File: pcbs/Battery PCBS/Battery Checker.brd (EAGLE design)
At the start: 49.5 x 49.5 mm, 19 parts

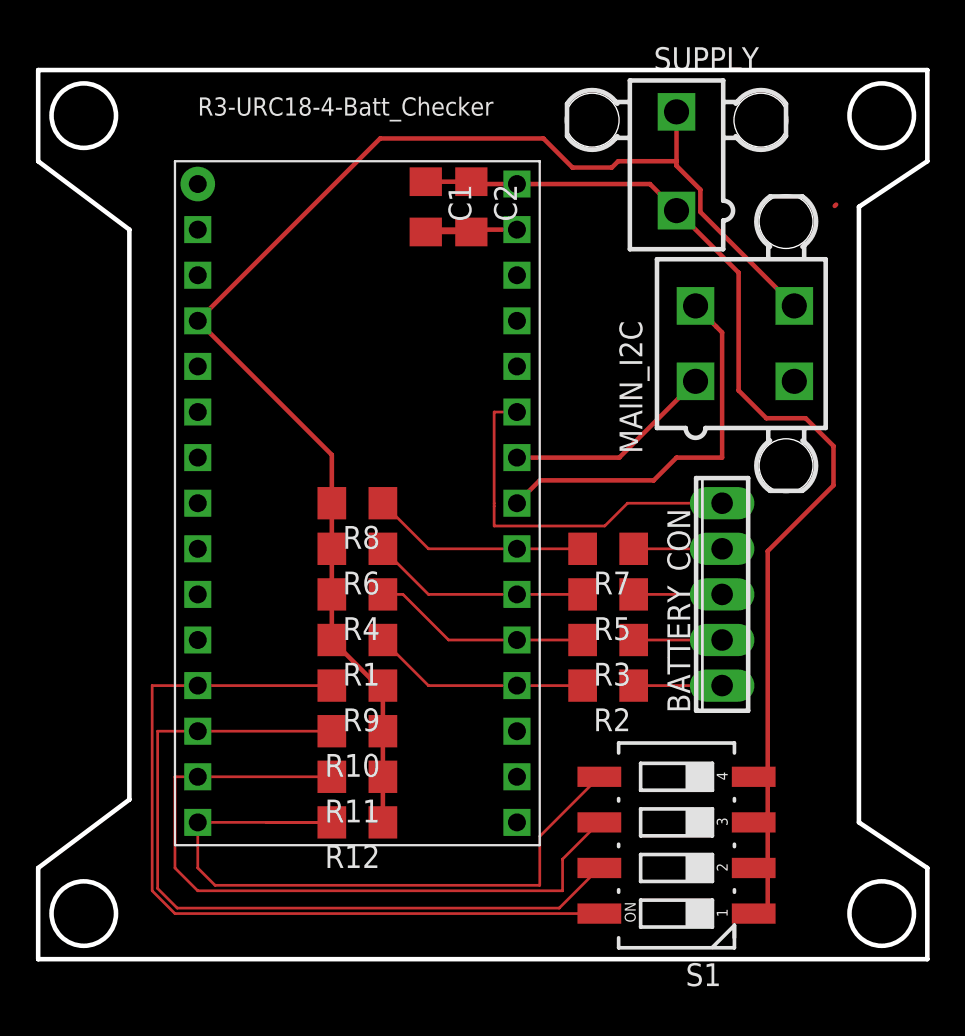
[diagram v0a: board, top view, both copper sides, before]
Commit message: added logic level converter
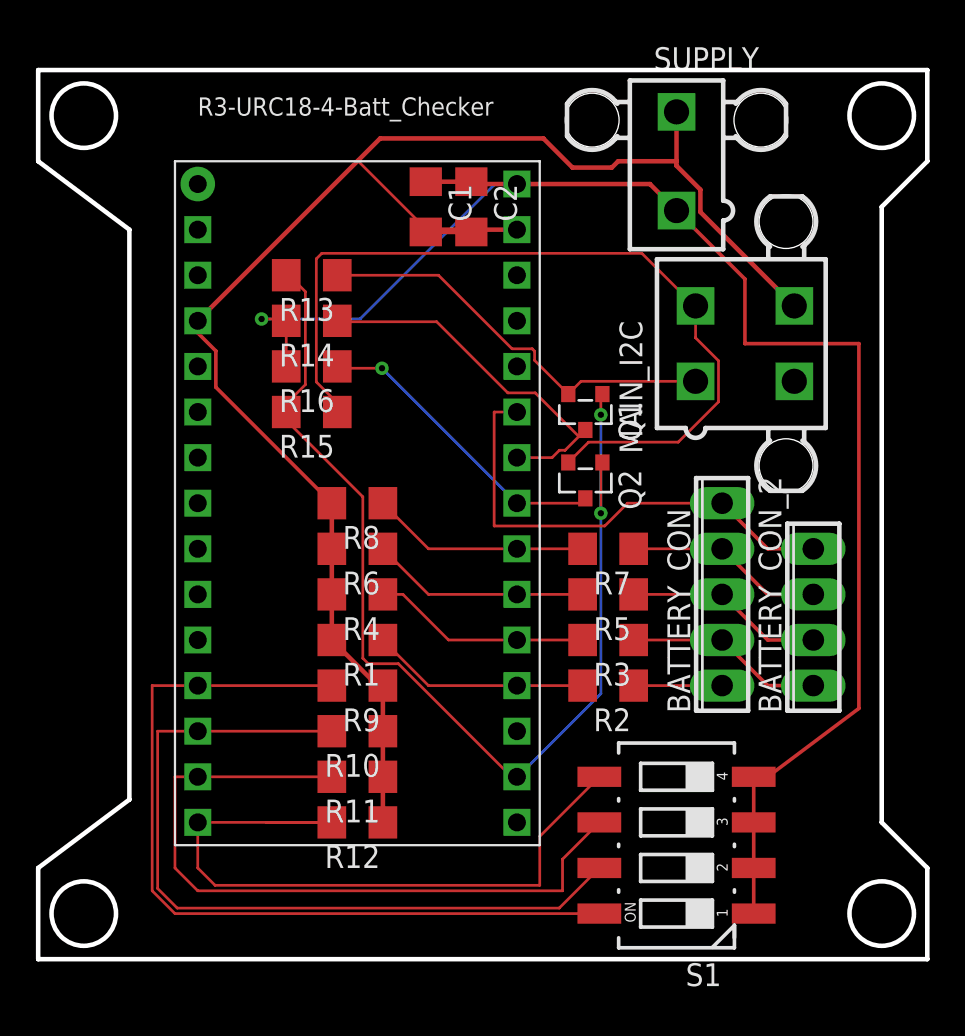
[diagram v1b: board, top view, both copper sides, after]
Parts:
- added BATTERY_CON_2: (no value), con-phoenix-254:4POL254
- added Q1, Q2: BSS138, bss138_10:SOT23
- added R13, R14, R15, R16: 10k, rcl:R1206
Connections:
- removed net 3.3V: U$1.3.3V
- new net 3.3: Q1.1, Q2.1, R13.2, R15.2, U$1.3.3V
- new net SCL_HV: Q1.3, R14.1, U$1.A5
- new net SDA_HV: Q2.3, R16.1, U$1.A4
- net BATT2: now also BATTERY_CON_2.1
- net BATT3: now also BATTERY_CON_2.2
- net BATT4: now also BATTERY_CON_2.3
- net BATT5: now also BATTERY_CON_2.4
- net SCL: now also Q1.2, R13.1; no longer U$1.A5
- net SDA: now also Q2.2, R15.1; no longer U$1.A4
- net VIN: now also R14.2, R16.2
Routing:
- net 3.3: track 0.00 -> 61.6 mm, vias 0 -> 2
- net SDA: track 21.5 -> 47.2 mm
- net VIN: track 62.4 -> 85.6 mm, vias 0 -> 1
- net SCL_HV: track 0.00 -> 21.1 mm
- net SDA_HV: track 0.00 -> 17.1 mm, vias 0 -> 1
- net SCL: track 11.7 -> 23.3 mm
- net GND: track 85.4 -> 91.5 mm
- net BATT5: track 20.8 -> 27.0 mm
- net BATT3: track 4.93 -> 11.1 mm
- net BATT2: track 4.93 -> 11.1 mm
- net BATT4: track 4.93 -> 11.1 mm
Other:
- outline, holes or cut-outs redrawn
